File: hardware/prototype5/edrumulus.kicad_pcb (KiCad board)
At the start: 2 copper layers, 65 x 56.5 mm, 67 parts, among them J1 Trigger Connector, J2 Raspberry Pi GPIO pins, U1 ESP32-DEVKIT-V1

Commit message: some layout cleanup
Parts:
- added C1: 100 nF, Capacitor_SMD:C_1206_3216Metric_Pad1.33x1.80mm_HandSolder, F.Cu at (209.0, 103.1)
- added C10: 100 nF, Capacitor_SMD:C_1206_3216Metric_Pad1.33x1.80mm_HandSolder, F.Cu at (199.2, 113.2)
- added C11: 100 nF, Capacitor_SMD:C_1206_3216Metric_Pad1.33x1.80mm_HandSolder, F.Cu at (205.5, 109.8)
- added C12: 100 nF, Capacitor_SMD:C_1206_3216Metric_Pad1.33x1.80mm_HandSolder, F.Cu at (192.8, 118.0)
- added C13: 100 nF, Capacitor_SMD:C_1206_3216Metric_Pad1.33x1.80mm_HandSolder, F.Cu at (199.5, 109.8)
- added C14: 100 nF, Capacitor_SMD:C_1206_3216Metric_Pad1.33x1.80mm_HandSolder, F.Cu at (186.8, 124.7)
- added C15: 100 nF, Capacitor_SMD:C_1206_3216Metric_Pad1.33x1.80mm_HandSolder, F.Cu at (215.1, 103.1)
- added C16: 1 µF, Capacitor_SMD:C_1206_3216Metric_Pad1.33x1.80mm_HandSolder, F.Cu at (193.2, 114.6)
- added C17: 22 µF, Capacitor_SMD:C_1206_3216Metric_Pad1.33x1.80mm_HandSolder, F.Cu at (186.8, 121.3)
- added C18: 10 nF, Capacitor_SMD:C_1206_3216Metric_Pad1.33x1.80mm_HandSolder, F.Cu at (180.8, 117.9)
- added C19: 10 µF, Capacitor_SMD:C_1206_3216Metric_Pad1.33x1.80mm_HandSolder, F.Cu at (180.8, 124.6)
- added C2: 100 nF, Capacitor_SMD:C_1206_3216Metric_Pad1.33x1.80mm_HandSolder, F.Cu at (187.2, 114.6)
- added C20: 1 µF, Capacitor_SMD:C_1206_3216Metric_Pad1.33x1.80mm_HandSolder, F.Cu at (193.5, 109.7)
- added C21: 22 µF, Capacitor_SMD:C_1206_3216Metric_Pad1.33x1.80mm_HandSolder, F.Cu at (203.0, 103.1)
- added C3: 100 nF, Capacitor_SMD:C_1206_3216Metric_Pad1.33x1.80mm_HandSolder, F.Cu at (190.7, 106.4)
- added C4: 100 nF, Capacitor_SMD:C_1206_3216Metric_Pad1.33x1.80mm_HandSolder, F.Cu at (197.0, 103.1)
- added C5: 100 nF, Capacitor_SMD:C_1206_3216Metric_Pad1.33x1.80mm_HandSolder, F.Cu at (180.8, 121.2)
- added C6: 100 nF, Capacitor_SMD:C_1206_3216Metric_Pad1.33x1.80mm_HandSolder, F.Cu at (186.8, 118.0)
- added C7: 100 nF, Capacitor_SMD:C_1206_3216Metric_Pad1.33x1.80mm_HandSolder, F.Cu at (199.5, 106.5)
- added C8: 100 nF, Capacitor_SMD:C_1206_3216Metric_Pad1.33x1.80mm_HandSolder, F.Cu at (205.5, 106.5)
- added C9: 100 nF, Capacitor_SMD:C_1206_3216Metric_Pad1.33x1.80mm_HandSolder, F.Cu at (192.8, 121.3)
- added D27: BAT85, Diode_SMD:D_MiniMELF, F.Cu at (190.8, 103.1)
- added D28: BAT85, Diode_SMD:D_MiniMELF, F.Cu at (181.0, 111.3)
- added D29: BAT85, Diode_SMD:D_MiniMELF, F.Cu at (187.3, 111.3)
- added D30: BAT85, Diode_SMD:D_MiniMELF, F.Cu at (181.0, 114.6)
- added D31: BOARD-LED, LED_SMD:LED_0603_1608Metric, F.Cu at (220.1, 102.7)
- added R39: 22 kOhm, Resistor_SMD:R_1206_3216Metric_Pad1.30x1.75mm_HandSolder, F.Cu at (198.8, 123.1)
- added R40: 22 kOhm, Resistor_SMD:R_1206_3216Metric_Pad1.30x1.75mm_HandSolder, F.Cu at (211.5, 109.7)
- added R41: 22 kOhm, Resistor_SMD:R_1206_3216Metric_Pad1.30x1.75mm_HandSolder, F.Cu at (205.2, 116.4)
- added R42: 22 kOhm, Resistor_SMD:R_1206_3216Metric_Pad1.30x1.75mm_HandSolder, F.Cu at (205.2, 113.1)
- added R43: 22 kOhm, Resistor_SMD:R_1206_3216Metric_Pad1.30x1.75mm_HandSolder, F.Cu at (211.5, 106.4)
- added R44: 22 kOhm, Resistor_SMD:R_1206_3216Metric_Pad1.30x1.75mm_HandSolder, F.Cu at (198.8, 119.8)
- added R45: 10 kOhm, Resistor_SMD:R_1206_3216Metric_Pad1.30x1.75mm_HandSolder, F.Cu at (199.2, 116.5)
- added R46: 470 Ohm, Resistor_SMD:R_1206_3216Metric_Pad1.30x1.75mm_HandSolder, F.Cu at (192.8, 124.6)
- added U2: AMS1117-3.3, Package_TO_SOT_SMD:SOT-223-3_TabPin2, F.Cu at (182.7, 105.6)
- added U3: LT1761-3.3, Package_TO_SOT_SMD:TSOT-23-5, F.Cu at (217.1, 107.0)
- R27, R28: value 100 kOhm -> 22 kOhm
- R30, R32, R35, R36: value 22 kOhm -> 100 kOhm
- U1: value ESP32-DEVKIT-V1 -> ESP32-WROOM-32U; footprint edrumulus:esp32_devkit_v1 -> RF_Module:ESP32-WROOM-32U
- moved U1 62.4 mm to (186.4, 80.8)
- moved D25 54.2 mm to (77.7, 122.2)
- moved D26 54.2 mm to (80.3, 122.2)
- moved R37 54.2 mm to (85.3, 122.4)
- moved R38 54.2 mm to (82.8, 122.4)
- moved R18 34.8 mm to (85.3, 71.1)
- moved D2 34.8 mm to (85.3, 76.7)
- moved R10 34.8 mm to (82.8, 76.7)
- moved D10 34.8 mm to (82.8, 71.3)
- moved R1 32.7 mm to (80.0, 77.0)
- moved D19 32.3 mm to (83.4, 110.8)
- moved D23 32.3 mm to (80.8, 105.1)
- moved R27 32.3 mm to (78.5, 111.0)
- moved R31 32.3 mm to (81.0, 111.0)
- moved R35 32.3 mm to (83.4, 104.9)
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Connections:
- D18 pad 1: GPIO15 -> GPIO2
- D19 pad 1: GPIO39 -> 3V3
- D19 pad 2: CRASH1-SLEEVE -> GPIO2
- D22 pad 1: 3V3 -> GPIO15
- D22 pad 2: GPIO15 -> CRASH1-SLEEVE
- D23 pad 2: GPIO39 -> GPIO12
- D24 pad 2: GPIO12 -> GPIO15
- J1 pad 15: unconnected-(J1-Pad15) -> TOM1-RING
- J1 pad 25: unconnected-(J1-Pad25) -> RIDE-BELL-TIP
- J2 pad 2: ESP-VIN -> RASPI-VIN
- R25 pad 1: KICK-TIP -> GPIO33
- R25 pad 2: GPIO33 -> KICK-TIP
- R26 pad 1: TOM3-TIP -> RIDE-BELL-TIP
- R26 pad 2: GPIO15 -> GPIO2
- R27 pad 1: TOM1-TIP -> GPIO2
- R27 pad 2: GPIO39 -> CRASH1-SLEEVE
- R28 pad 1: TOM2-TIP -> 3V3
- R28 pad 2: GPIO12 -> GPIO2
- R30 pad 1: GPIO15 -> GPIO12
- R30 pad 2: CRASH1-SLEEVE -> TOM2-TIP
- R31 pad 1: GPIO39 -> GPIO12
- R32 pad 1: GPIO12 -> GPIO15
- R32 pad 2: CRASH1-SLEEVE -> TOM3-TIP
- R34 pad 1: 3V3 -> GPIO15
- R34 pad 2: GPIO15 -> CRASH1-SLEEVE
- R35 pad 1: 3V3 -> TOM1-RING
- R35 pad 2: GPIO39 -> GPIO4
- R36 pad 1: 3V3 -> TOM1-TIP
- R36 pad 2: GPIO12 -> GPIO39
- U1 pad 1: unconnected-(U1-Pad1) -> CRASH1-SLEEVE
- U1 pad 10: GPIO27 -> GPIO25
- U1 pad 11: GPIO14 -> GPIO26
- U1 pad 12: GPIO12 -> GPIO27
- U1 pad 13: GPIO13 -> GPIO14
- U1 pad 14: CRASH1-SLEEVE -> GPIO12
- U1 pad 15: ESP-VIN -> CRASH1-SLEEVE
- U1 pad 16: 3V3 -> GPIO13
- U1 pad 17: CRASH1-SLEEVE -> unconnected-(U1-Pad17)
- U1 pad 18: GPIO15 -> unconnected-(U1-Pad18)
- U1 pad 2: GPIO36 -> ESP32-3V3
- U1 pad 23: unconnected-(U1-Pad23) -> GPIO15
- U1 pad 24: unconnected-(U1-Pad24) -> GPIO2
- U1 pad 26: unconnected-(U1-Pad26) -> GPIO4
- U1 pad 27: ESP-UART0-RX -> unconnected-(U1-Pad27)
- U1 pad 28: ESP-UART0-TX -> unconnected-(U1-Pad28)
- U1 pad 29: unconnected-(U1-Pad29) -> Net-(R46-Pad1)
- U1 pad 3: GPIO39 -> Net-(C20-Pad1)
- U1 pad 4: GPIO34 -> GPIO36
- U1 pad 5: GPIO35 -> GPIO39
- U1 pad 6: GPIO32 -> GPIO34
- U1 pad 7: GPIO33 -> GPIO35
- U1 pad 8: GPIO25 -> GPIO32
- U1 pad 9: GPIO26 -> GPIO33
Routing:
- net CRASH1-SLEEVE: track 350.1 -> 130.4 mm, vias 3 -> 0
- net 3V3: track 206.6 -> 26.2 mm, vias 2 -> 0
- net GPIO15: track 127.4 -> 2.34 mm, vias 1 -> 0
- net ESP-VIN: track 86.6 -> 0.00 mm
- net GPIO33: track 82.9 -> 7.83 mm, vias 1 -> 0
- net GPIO39: track 74.0 -> 0.00 mm, vias 1 -> 0
- net HI-HAT-RING: track 70.2 -> 0.00 mm
- net SNARE-RING: track 70.0 -> 0.00 mm
- net CRASH1-TIP: track 63.3 -> 0.00 mm
- net HI-HAT-TIP: track 60.5 -> 0.00 mm
- net GPIO13: track 66.5 -> 6.98 mm, vias 1 -> 0
- net GPIO27: track 62.6 -> 8.14 mm, vias 1 -> 0
- net SNARE-TIP: track 52.3 -> 0.00 mm
- net GPIO12: track 49.0 -> 0.00 mm, vias 1 -> 0
- net RIDE-TIP: track 47.4 -> 0.00 mm
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- removed copper zone on B.Cu, net CRASH1-SLEEVE
- removed copper zone on F.Cu, net CRASH1-SLEEVE

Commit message: some more prototype 5 development
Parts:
- C6, D15, D7, R15, R23, U3: moved to B.Cu
- J1: footprint Connector_Dsub:DSUB-25_Female_Vertical_P2.77x2.84mm -> Connector_Dsub:DSUB-25_Female_Horizontal_P2.77x2.84mm_EdgePinOffset7.70mm_Housed_MountingHolesOffset9.12mm
- moved R39 111.5 mm to (101.4, 68.8), turned to -90 degrees
- moved U3 105.1 mm to (114.1, 86.2), turned to 180 degrees
- moved C15 96.8 mm to (120.3, 83.4)
- moved D16 74.5 mm to (85.4, 136.7)
- moved D8 74.5 mm to (78.7, 139.9)
- moved R16 74.5 mm to (81.3, 139.7)
- moved R24 74.5 mm to (85.4, 139.2)
- moved R8 71.1 mm to (72.6, 138.4)
- moved D31 70.0 mm to (150.6, 111.1)
- moved C6 63.9 mm to (127.9, 93.3), turned to 90 degrees
- moved R17 62.2 mm to (190.0, 144.2)
- moved D1 62.2 mm to (190.0, 149.6)
- moved D9 62.2 mm to (186.7, 144.5)
- moved R3 62.2 mm to (194.1, 150.4)
- moved R9 62.2 mm to (186.7, 149.9)
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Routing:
- net CRASH1-SLEEVE: track 130.4 -> 117.0 mm
- net GPIO34: track 11.8 -> 0.00 mm
- net 3V3: track 26.2 -> 18.5 mm
- net GPIO13: track 6.98 -> 0.00 mm
- net GPIO14: track 12.7 -> 8.15 mm
- net GPIO15: track 2.34 -> 0.00 mm
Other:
- board text added: "Edrumulus Prototype 5"
- board text removed: "Edrumulus Prototype 4"

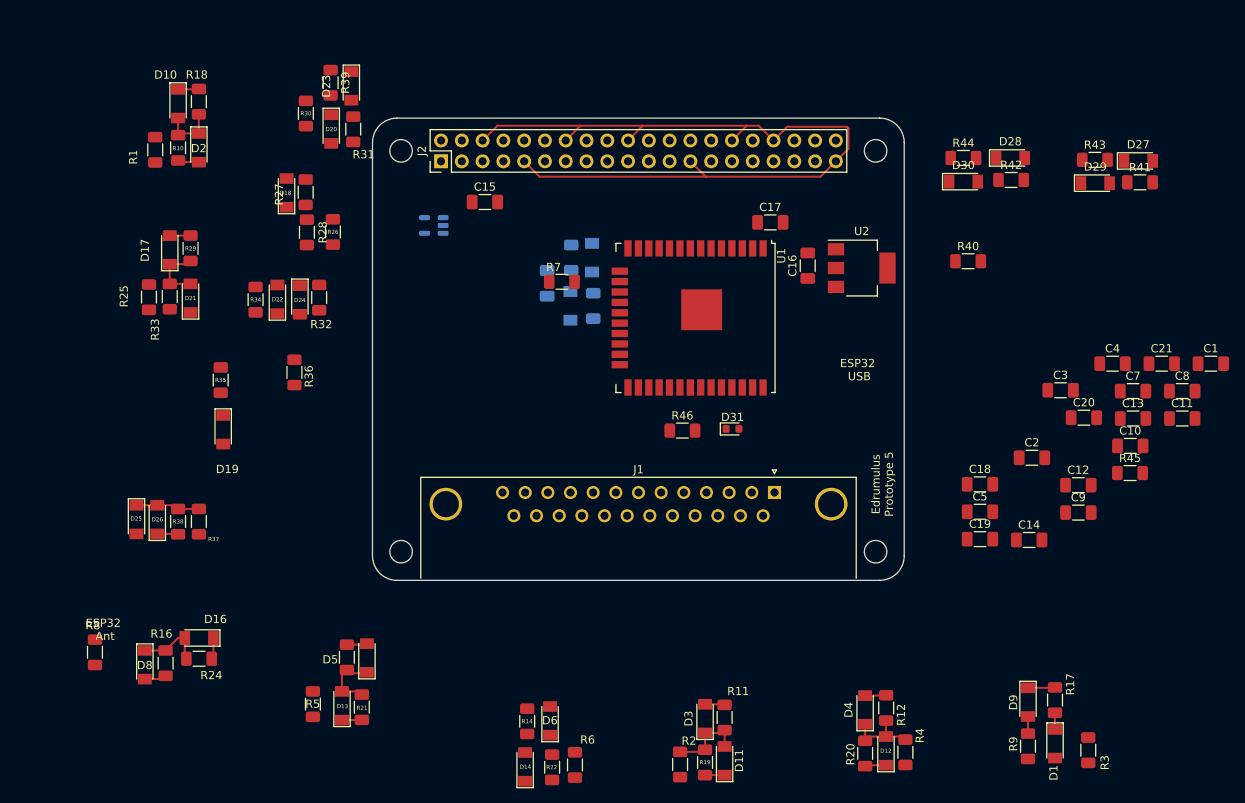
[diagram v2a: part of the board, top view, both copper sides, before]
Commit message: some more layout cleanup for prototype 5
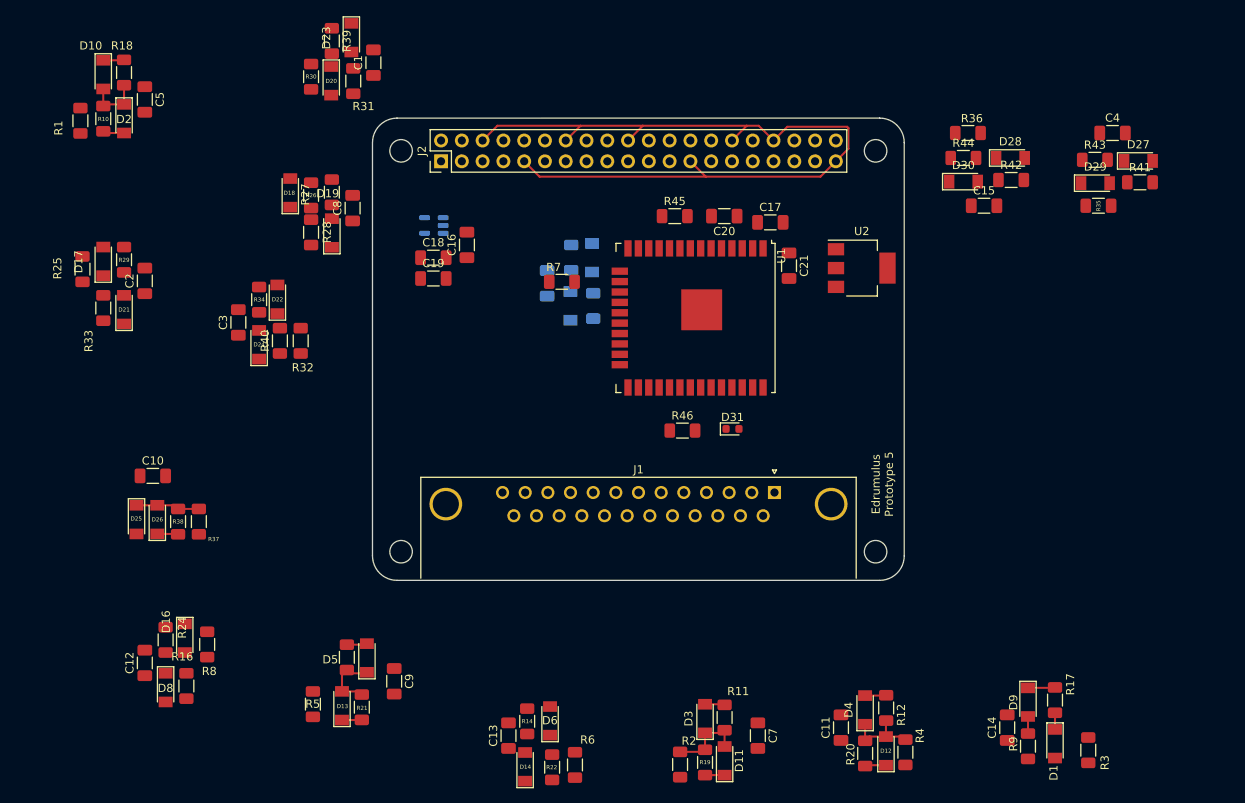
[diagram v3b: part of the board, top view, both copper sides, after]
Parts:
- moved C10 119.5 mm to (79.7, 116.8)
- moved C12 116.2 mm to (78.7, 139.7), turned to 90 degrees
- moved C5 113.8 mm to (78.7, 70.8), turned to -90 degrees
- moved C2 110.6 mm to (78.7, 93.0), turned to 90 degrees
- moved R35 109.4 mm to (195.3, 83.8), turned to 0 degrees
- moved C1 108.8 mm to (106.7, 66.3), turned to 90 degrees
- moved C8 103.8 mm to (104.1, 84.1), turned to 90 degrees
- moved C3 100.8 mm to (90.2, 98.1), turned to 90 degrees
- moved R36 87.4 mm to (179.3, 74.9), turned to 0 degrees
- moved C9 86.1 mm to (109.2, 141.9), turned to -90 degrees
- moved C13 85.6 mm to (123.2, 148.6), turned to 90 degrees
- moved R40 84.7 mm to (95.2, 100.3), turned to 90 degrees
- moved C19 74.0 mm to (114.0, 92.7)
- moved C18 72.3 mm to (114.0, 90.2)
- moved R45 63.9 mm to (143.5, 85.1)
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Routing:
- net GPIO27: track 8.14 -> 0.00 mm
- net GPIO33: track 7.83 -> 0.75 mm
- net CRASH1-SLEEVE: track 117.0 -> 111.8 mm
- net 3V3: track 18.5 -> 15.9 mm
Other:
- board text removed: "ESP32 Ant"
- board text removed: "ESP32 USB"

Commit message: some more compenent sorting for prototype 5
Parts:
- C6, D15, D7, R15, R23: moved to F.Cu
- J1: moved to B.Cu
- moved R1 135.1 mm to (201.9, 40.6)
- moved C5 134.3 mm to (209.6, 40.3)
- moved D10 134.3 mm to (204.5, 37.3)
- moved D2 134.3 mm to (207.0, 42.7)
- moved R10 134.3 mm to (204.5, 42.7)
- moved R18 134.3 mm to (207.0, 37.1)
- moved R2 126.9 mm to (110.5, 29.7)
- moved C7 125.0 mm to (118.2, 28.8)
- moved R11 124.6 mm to (115.4, 26.5)
- moved R19 124.6 mm to (113.0, 32.0)
- moved D11 124.6 mm to (115.4, 31.8)
- moved D3 124.6 mm to (113.0, 26.7)
- moved R4 121.8 mm to (149.8, 30.8)
- moved R3 121.5 mm to (166.3, 32.0)
- moved C11 121.0 mm to (141.8, 28.6)
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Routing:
- net 3V3: track 15.9 -> 5.12 mm
- net GPIO26: track 9.73 -> 0.00 mm
- net GPIO32: track 9.27 -> 0.00 mm
- net GPIO14: track 8.15 -> 0.00 mm
- net CRASH1-SLEEVE: track 111.8 -> 106.8 mm
- net GPIO35: track 4.12 -> 0.00 mm
- net GPIO33: track 0.75 -> 0.19 mm

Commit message: more work on prototype 5
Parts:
- C1, C11, C12, C13, C14, C15, C2, C3, C4, C5, C6, C7, C8, C9, D1, D10, D11, D12, D13, D14, D15, D16, D17, D18, D19, D2, D20, D21, D22, D23, D24, D27, D28, D29, D3, D30, D4, D5, D6, D7, D8, D9, R10, R11, R12, R13, R14, R15, R16, R17, R18, R19, R20, R21, R22, R23, R24, R27, R28, R29, R31, R33, R34, R39, R40, R41, R42, R43, R44, R9: moved to B.Cu
- J1: moved to F.Cu
- moved C5 66.7 mm to (163.6, 88.8)
- moved D28 63.7 mm to (158.4, 91.5), turned to -90 degrees
- moved D2 63.5 mm to (166.4, 91.5)
- moved R18 62.6 mm to (166.4, 84.6)
- moved R10 60.2 mm to (168.9, 91.3)
- moved R42 60.0 mm to (161.0, 91.4), turned to -90 degrees
- moved D10 59.2 mm to (168.9, 84.6)
- moved C15 55.7 mm to (155.5, 87.5), turned to -90 degrees
- moved R36 55.3 mm to (161.0, 83.8), turned to 180 degrees
- moved R1 54.4 mm to (168.9, 83.8), turned to 180 degrees
- moved R44 53.7 mm to (158.4, 83.3), turned to -90 degrees
- moved D30 49.9 mm to (161.0, 83.3), turned to -90 degrees
- moved J1 39.5 mm to (155.7, 119.0), turned to 0 degrees
- moved R2 24.4 mm to (122.0, 51.3)
- moved D3 20.5 mm to (119.5, 46.2)
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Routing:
- net SNARE-TIP: track 0.00 -> 43.6 mm
- net GPIO36: track 7.05 -> 32.1 mm, vias 0 -> 1
- net GPIO39: track 0.00 -> 23.3 mm, vias 0 -> 1
- net CRASH1-SLEEVE: track 106.8 -> 121.4 mm
- net 3V3: track 5.12 -> 7.80 mm

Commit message: some prototype 5 routing
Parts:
- moved R29 67.9 mm to (134.1, 91.1), turned to -90 degrees
- moved D17 67.8 mm to (131.8, 91.3), turned to -90 degrees
- moved C14 64.3 mm to (142.1, 87.5)
- moved R9 63.4 mm to (144.9, 91.2)
- moved D1 62.0 mm to (147.2, 91.4)
- moved C2 61.6 mm to (129.1, 87.5), turned to -90 degrees
- moved D9 61.2 mm to (144.8, 83.4)
- moved R25 59.8 mm to (135.6, 84.3), turned to 0 degrees
- moved R17 59.4 mm to (147.2, 83.3)
- moved R14 59.0 mm to (150.4, 91.2), turned to -90 degrees
- moved D6 56.4 mm to (152.7, 91.5), turned to -90 degrees
- moved D21 54.3 mm to (134.0, 83.6), turned to -90 degrees
- moved R33 54.2 mm to (131.7, 83.4), turned to -90 degrees
- moved R3 53.9 mm to (148.9, 83.8), turned to 0 degrees
- moved D4 49.8 mm to (137.0, 91.4), turned to -90 degrees
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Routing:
- net CRASH1-TIP: track 0.00 -> 92.9 mm
- net TOM1-TIP: track 0.00 -> 52.5 mm
- net GPIO33: track 0.19 -> 15.9 mm, vias 0 -> 1
- net GPIO32: track 0.00 -> 11.2 mm, vias 0 -> 1
- net GPIO34: track 0.00 -> 11.1 mm, vias 0 -> 1
- net GPIO35: track 0.00 -> 8.70 mm, vias 0 -> 1
- net CRASH1-SLEEVE: track 121.4 -> 113.4 mm
- net GPIO36: track 32.1 -> 29.0 mm
- net SNARE-TIP: track 43.6 -> 42.6 mm
- net GPIO39: track 23.3 -> 22.7 mm

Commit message: prototype 5 component placement
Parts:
- removed C11, C12, C13, C5, C6, C7, C8, C9: 100 nF, Capacitor_SMD:C_1206_3216Metric_Pad1.33x1.80mm_HandSolder
- C10, D25, D26, R37, R38: moved to B.Cu
- moved D25 89.8 mm to (162.6, 109.3)
- moved D23 89.5 mm to (116.8, 109.7), turned to 90 degrees
- moved R39 85.9 mm to (114.4, 109.5), turned to 90 degrees
- moved C10 85.9 mm to (160.6, 103.9), turned to 180 degrees
- moved D26 84.9 mm to (160.0, 109.3)
- moved C1 83.2 mm to (112.1, 106.2), turned to -90 degrees
- moved R31 80.4 mm to (117.0, 102.1), turned to 90 degrees
- moved R38 80.0 mm to (157.5, 109.5)
- moved D20 76.6 mm to (114.3, 102.1), turned to 90 degrees
- moved R30 75.9 mm to (117.0, 101.2), turned to 90 degrees
- moved R37 75.1 mm to (154.9, 109.5)
- moved R27 71.0 mm to (131.8, 101.9)
- moved D18 71.0 mm to (134.4, 102.1)
- moved D19 70.9 mm to (131.8, 109.7)
- moved R28 70.9 mm to (134.4, 109.6)
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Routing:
- net GPIO12: track 0.00 -> 58.3 mm, vias 0 -> 1
- net GPIO14: track 0.00 -> 36.2 mm, vias 0 -> 1
- net GPIO13: track 0.00 -> 26.4 mm, vias 0 -> 1
- net GPIO27: track 0.00 -> 26.4 mm, vias 0 -> 1
- net GPIO26: track 0.00 -> 21.3 mm, vias 0 -> 1
- net GPIO15: track 0.00 -> 15.0 mm, vias 0 -> 1
- net GPIO4: track 0.00 -> 7.48 mm, vias 0 -> 1
- net GPIO2: track 0.00 -> 7.16 mm, vias 0 -> 1

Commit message: more prototype 5 routing
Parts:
- moved U3 11.8 mm to (110.5, 97.8)
- moved R25 2.14 mm to (133.5, 83.6)
- moved R20 1.61 mm to (135.6, 82.7)
- moved D21 1.01 mm to (133.3, 82.9)
- moved R33 0.95 mm to (131.0, 82.7)
- moved D12 0.68 mm to (139.4, 82.9)
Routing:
- net HI-HAT-TIP: track 0.00 -> 100.4 mm, vias 0 -> 1
- net SNARE-RING: track 0.00 -> 77.6 mm, vias 0 -> 1
- net ESP-UART0-TX: track 0.00 -> 75.4 mm, vias 0 -> 1
- net ESP-UART0-RX: track 0.00 -> 67.4 mm, vias 0 -> 1
- net GPIO12: track 58.3 -> 36.9 mm
- net TOM1-RING: track 0.00 -> 19.1 mm
- net RIDE-BELL-TIP: track 0.00 -> 17.0 mm
- net GPIO14: track 36.2 -> 29.8 mm
- net GPIO33: track 15.9 -> 19.3 mm
- net GPIO32: track 11.2 -> 13.9 mm
- net GPIO27: track 26.4 -> 24.6 mm
- net GPIO39: track 22.7 -> 21.8 mm
- net GPIO26: track 21.3 -> 20.7 mm
